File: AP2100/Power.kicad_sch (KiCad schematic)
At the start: 35 parts, among them U4 MPQ8634AGLE-P, U5 MPQ8634AGLE-P

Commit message: Add partsbox.io bom generator script
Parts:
- R24, R25: footprint (none) -> Resistor_SMD:R_0603_1608Metric
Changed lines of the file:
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@@
-    )
-  )
-  (symbol (lib_id "AP2100-rescue:GND-Scott") (at -15.875 60.96 0) (unit 1)
-    (in_bom yes) (on_board yes)
-    (property "Reference" "#PWR0118" (id 0) (at -15.875 67.31 0)
-      (effects (font (size 1.27 1.27)) hide)
-    )
-    (property "Value" "GND" (id 1) (at -15.748 65.3542 0))
-    (property "Footprint" "" (id 2) (at -15.875 60.96 0)
-      (effects (font (size 1.27 1.27)) hide)
-    )
-    (property "Datasheet" "" (id 3) (at -15.875 60.96 0)
-      (effects (font (size 1.27 1.27)) hide)
-    )
-  )
-  (symbol (lib_id "AP2100-rescue:GND-Scott") (at -12.065 -12.7 0) (unit 1)
-    (in_bom yes) (on_board yes)
-    (property "Reference" "#PWR0115" (id 0) (at -12.065 -6.35 0)
-      (effects (font (size 1.27 1.27)) hide)
-    )
-    (property "Value" "GND" (id 1) (at -11.938 -8.3058 0))
-    (property "Footprint" "" (id 2) (at -12.065 -12.7 0)
-      (effects (font (size 1.27 1.27)) hide)
-    )
-    (property "Datasheet" "" (id 3) (at -12.065 -12.7 0)
-      (effects (font (size 1.27 1.27)) hide)
-    )
-  )
-  (symbol (lib_id "AP2100-rescue:GND-Scott") (at -1.27 -12.7 0) (unit 1)
-    (in_bom yes) (on_board yes)
-    (property "Reference" "#PWR0116" (id 0) (at -1.27 -6.35 0)
-      (effects (font (size 1.27 1.27)) hide)
-    )
-    (property "Value" "GND" (id 1) (at -1.143 -8.3058 0))
-    (property "Footprint" "" (id 2) (at -1.27 -12.7 0)
-      (effects (font (size 1.27 1.27)) hide)
-    )
-    (property "Datasheet" "" (id 3) (at -1.27 -12.7 0)
-      (effects (font (size 1.27 1.27)) hide)
     )
   )
@@
       (effects (font (size 1.27 1.27)) (justify left))
     )
-    (property "Footprint" "" (id 2) (at 86.995 140.335 0)
+    (property "Footprint" "Resistor_SMD:R_0603_1608Metric" (id 2) (at 86.995 140.335 0)
       (effects (font (size 1.27 1.27)) hide)
     )
@@
       (effects (font (size 1.27 1.27)) (justify left))
     )
-    (property "Footprint" "" (id 2) (at 94.615 135.89 0)
-      (effects (font (size 1.27 1.27)) hide)
-    )
+    (property "Footprint" "Resistor_SMD:R_0603_1608Metric" (id 2) (at 94.615 135.89 0)
+      (effects (font (size 1.27 1.27)) hide)
+    )

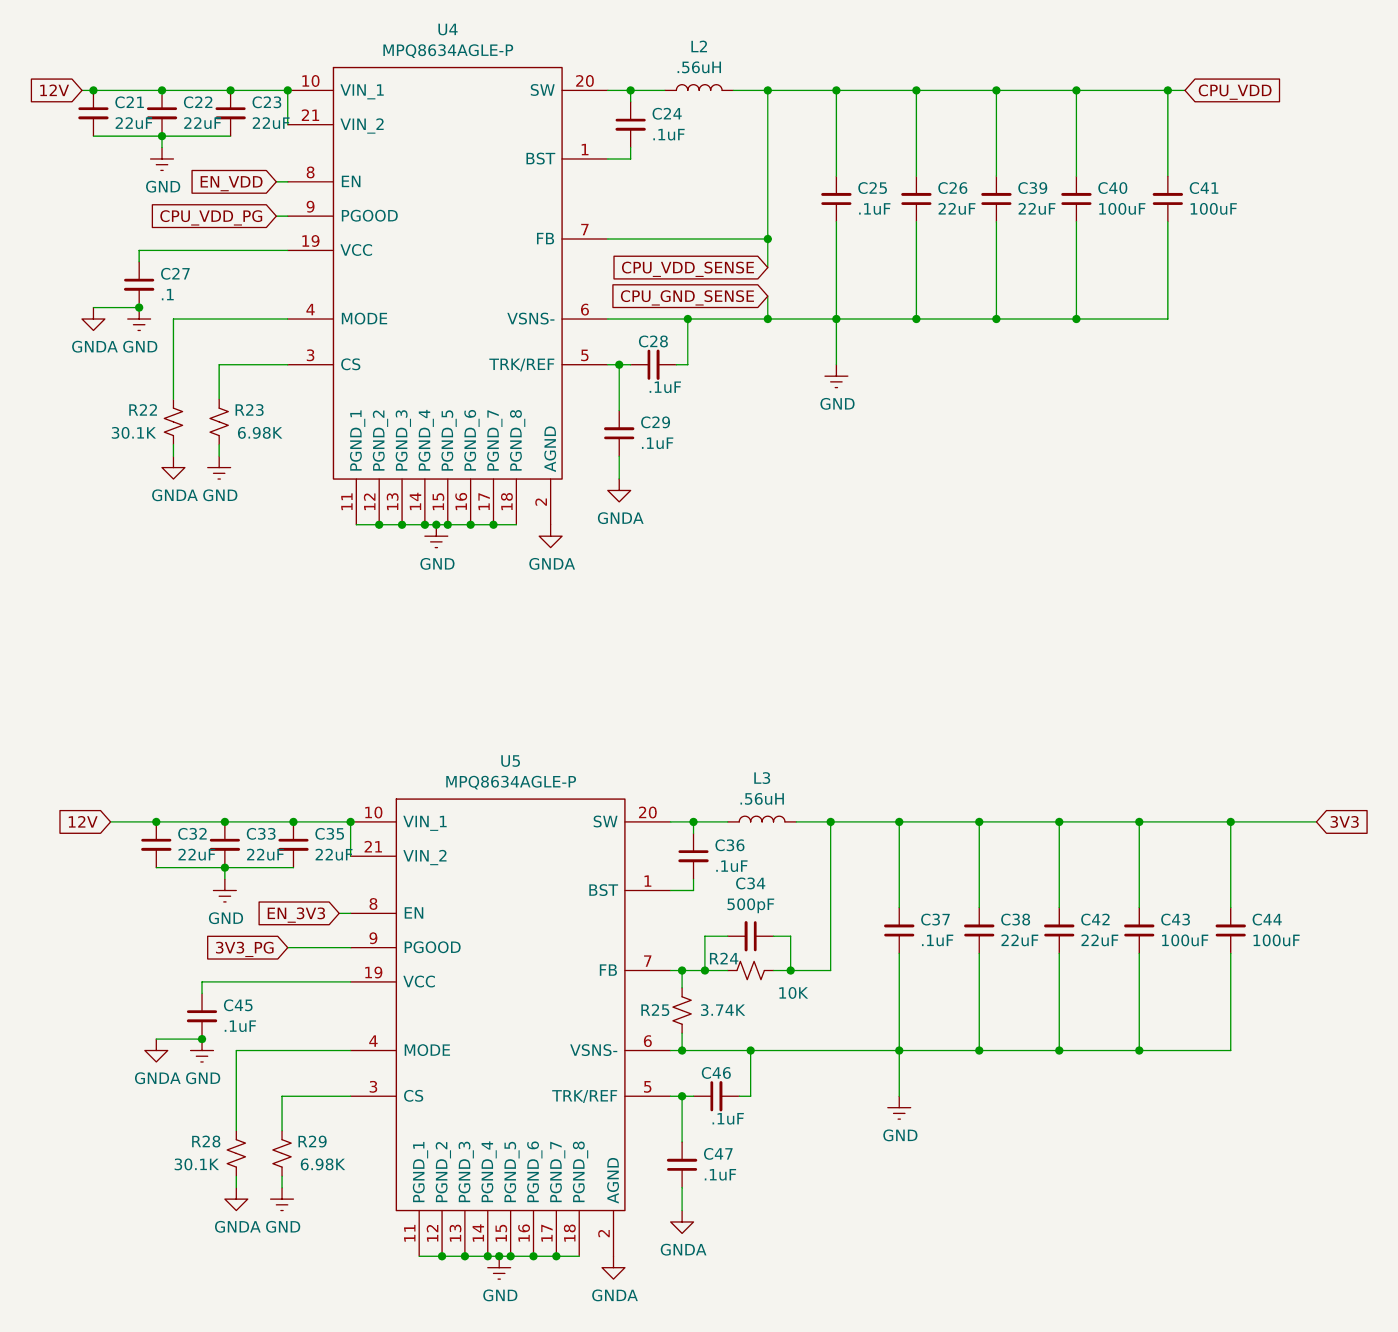
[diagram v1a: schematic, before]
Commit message: Add PartsBox part numbers to everything so far
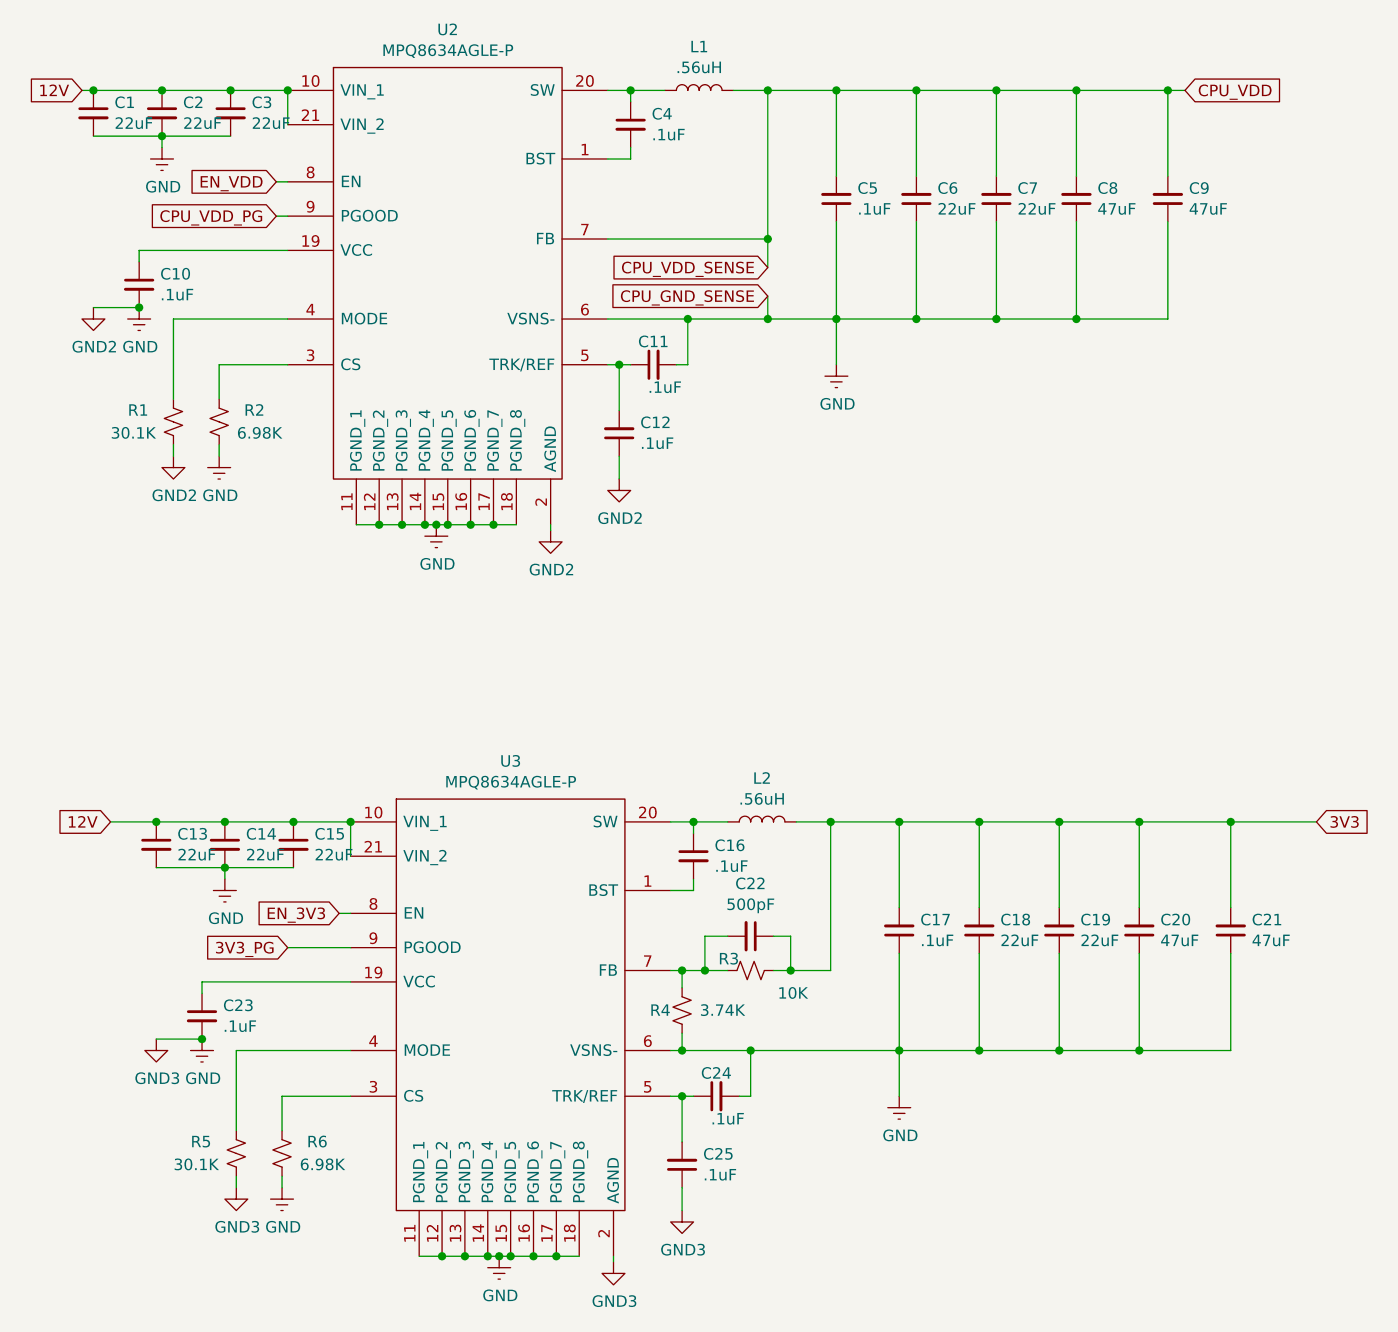
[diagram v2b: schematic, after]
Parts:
- C1: renamed from C21; footprint Capacitor_SMD:C_0805_2012Metric -> Capacitor_SMD:C_1210_3225Metric; PartsBoxID (none) -> 1210-22uF-X7R-25V
- C10: renamed from C27; value .1 -> .1uF; footprint Capacitor_SMD:C_0402_1005Metric -> Capacitor_SMD:C_0603_1608Metric; PartsBoxID (none) -> 0603-.1uF-X7R-25V
- C11: renamed from C28; footprint Capacitor_SMD:C_0402_1005Metric -> Capacitor_SMD:C_0603_1608Metric; PartsBoxID (none) -> 0603-.1uF-X7R-25V
- C12: renamed from C29; footprint Capacitor_SMD:C_0402_1005Metric -> Capacitor_SMD:C_0603_1608Metric; PartsBoxID (none) -> 0603-.1uF-X7R-25V
- C13: renamed from C32; footprint Capacitor_SMD:C_0805_2012Metric -> Capacitor_SMD:C_1210_3225Metric; PartsBoxID (none) -> 1210-22uF-X7R-25V; SPN - -> 22uF; SPR - -> Capacitor_SMD:C_1210_3225Metric; SPURL - -> (none)
- C14: renamed from C33; footprint Capacitor_SMD:C_0805_2012Metric -> Capacitor_SMD:C_1210_3225Metric; PartsBoxID (none) -> 1210-22uF-X7R-25V; SPN - -> 22uF; SPR - -> Capacitor_SMD:C_1210_3225Metric; SPURL - -> (none)
- C15: renamed from C35; footprint Capacitor_SMD:C_0805_2012Metric -> Capacitor_SMD:C_1210_3225Metric; PartsBoxID (none) -> 1210-22uF-X7R-25V; SPN - -> 22uF; SPR - -> Capacitor_SMD:C_1210_3225Metric; SPURL - -> (none)
- C16: renamed from C36; footprint Capacitor_SMD:C_0402_1005Metric -> Capacitor_SMD:C_0603_1608Metric; PartsBoxID (none) -> 0603-.1uF-X7R-25V
- C17: renamed from C37; footprint Capacitor_SMD:C_0402_1005Metric -> Capacitor_SMD:C_0603_1608Metric; PartsBoxID (none) -> 0603-.1uF-X7R-25V
- C18: renamed from C38; footprint Capacitor_SMD:C_0805_2012Metric -> Capacitor_SMD:C_1210_3225Metric; PartsBoxID (none) -> 1210-22uF-X7R-25V; SPN - -> 22uF; SPR - -> Capacitor_SMD:C_1210_3225Metric; SPURL - -> (none)
- C19: renamed from C42; footprint Capacitor_SMD:C_0805_2012Metric -> Capacitor_SMD:C_1210_3225Metric; PartsBoxID (none) -> 1210-22uF-X7R-25V; SPN - -> 22uF; SPR - -> Capacitor_SMD:C_1210_3225Metric; SPURL - -> (none)
- C2: renamed from C22; footprint Capacitor_SMD:C_0805_2012Metric -> Capacitor_SMD:C_1210_3225Metric; PartsBoxID (none) -> 1210-22uF-X7R-25V
- C20: renamed from C43; value 100uF -> 47uF; PartsBoxID (none) -> 1210-47uF-X5R-16V
- C21: renamed from C44; value 100uF -> 47uF; PartsBoxID (none) -> 1210-47uF-X5R-16V
- C22: renamed from C34; footprint Capacitor_SMD:C_0402_1005Metric -> Capacitor_SMD:C_0603_1608Metric; PartsBoxID (none) -> 0603-500pF-X7R-25V
- C23: renamed from C45; footprint Capacitor_SMD:C_0402_1005Metric -> Capacitor_SMD:C_0603_1608Metric; PartsBoxID (none) -> 0603-.1uF-X7R-25V
- C24: renamed from C46; footprint Capacitor_SMD:C_0402_1005Metric -> Capacitor_SMD:C_0603_1608Metric; PartsBoxID (none) -> 0603-.1uF-X7R-25V
- C25: renamed from C47; footprint Capacitor_SMD:C_0402_1005Metric -> Capacitor_SMD:C_0603_1608Metric; PartsBoxID (none) -> 0603-.1uF-X7R-25V
- C3: renamed from C23; footprint Capacitor_SMD:C_0805_2012Metric -> Capacitor_SMD:C_1210_3225Metric; PartsBoxID (none) -> 1210-22uF-X7R-25V
- C4: renamed from C24; footprint Capacitor_SMD:C_0402_1005Metric -> Capacitor_SMD:C_0603_1608Metric; PartsBoxID (none) -> 0603-.1uF-X7R-25V
- C5: renamed from C25; footprint Capacitor_SMD:C_0402_1005Metric -> Capacitor_SMD:C_0603_1608Metric; PartsBoxID (none) -> 0603-.1uF-X7R-25V
- C6: renamed from C26; footprint Capacitor_SMD:C_0805_2012Metric -> Capacitor_SMD:C_1210_3225Metric; PartsBoxID (none) -> 1210-22uF-X7R-25V; SPN - -> 22uF; SPR - -> Capacitor_SMD:C_1210_3225Metric; SPURL - -> (none)
- C7: renamed from C39; footprint Capacitor_SMD:C_0805_2012Metric -> Capacitor_SMD:C_1210_3225Metric; PartsBoxID (none) -> 1210-22uF-X7R-25V; SPN - -> 22uF; SPR - -> Capacitor_SMD:C_1210_3225Metric; SPURL - -> (none)
- C8: renamed from C40; value 100uF -> 47uF; PartsBoxID (none) -> 1210-47uF-X5R-16V
- C9: renamed from C41; value 100uF -> 47uF; PartsBoxID (none) -> 1210-47uF-X5R-16V
- L1: renamed from L2; PartsBoxID (none) -> AMPLA1306S-R56MT
- L2: renamed from L3; PartsBoxID (none) -> AMPLA1306S-R56MT
- R1: renamed from R22; footprint Resistor_SMD:R_0402_1005Metric -> Resistor_SMD:R_0603_1608Metric; PartsBoxID (none) -> 0603-30.1K-1%
- R2: renamed from R23; footprint Resistor_SMD:R_0402_1005Metric -> Resistor_SMD:R_0603_1608Metric; PartsBoxID (none) -> 0603-6.98K-1%
- R3: renamed from R24; PartsBoxID (none) -> 0603-10K-1%
- R4: renamed from R25; PartsBoxID (none) -> 0603-3.7K-1%
- R5: renamed from R28; footprint Resistor_SMD:R_0402_1005Metric -> Resistor_SMD:R_0603_1608Metric; PartsBoxID (none) -> 0603-30.1K-1%
- R6: renamed from R29; footprint Resistor_SMD:R_0402_1005Metric -> Resistor_SMD:R_0603_1608Metric; PartsBoxID (none) -> 0603-6.98K-1%
- U2: renamed from U4; PartsBoxID (none) -> MPQ8634AGLE-P
- U3: renamed from U5; PartsBoxID (none) -> MPQ8634AGLE-P

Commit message: More work on memory
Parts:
- C1, C10, C11, C12, C13, C14, C15, C16, C17, C18, C19, C2, C20, C21, C23, C24, C25, C3, C4, C5, C6, C7, C8, C9, R1, R2, R5, R6: MFR - -> (none)
- L1, L2: MFR Abracon -> (none); PartsBoxID AMPLA1306S-R56MT -> HCMA1305-R56-R
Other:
- note added: "0.9V 8A"
- note added: "8A"
